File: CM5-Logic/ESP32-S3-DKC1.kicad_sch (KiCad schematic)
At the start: 9 parts, among them J5 SSW-120-01-G-S-LL, J8 SSW-120-01-G-S-LL

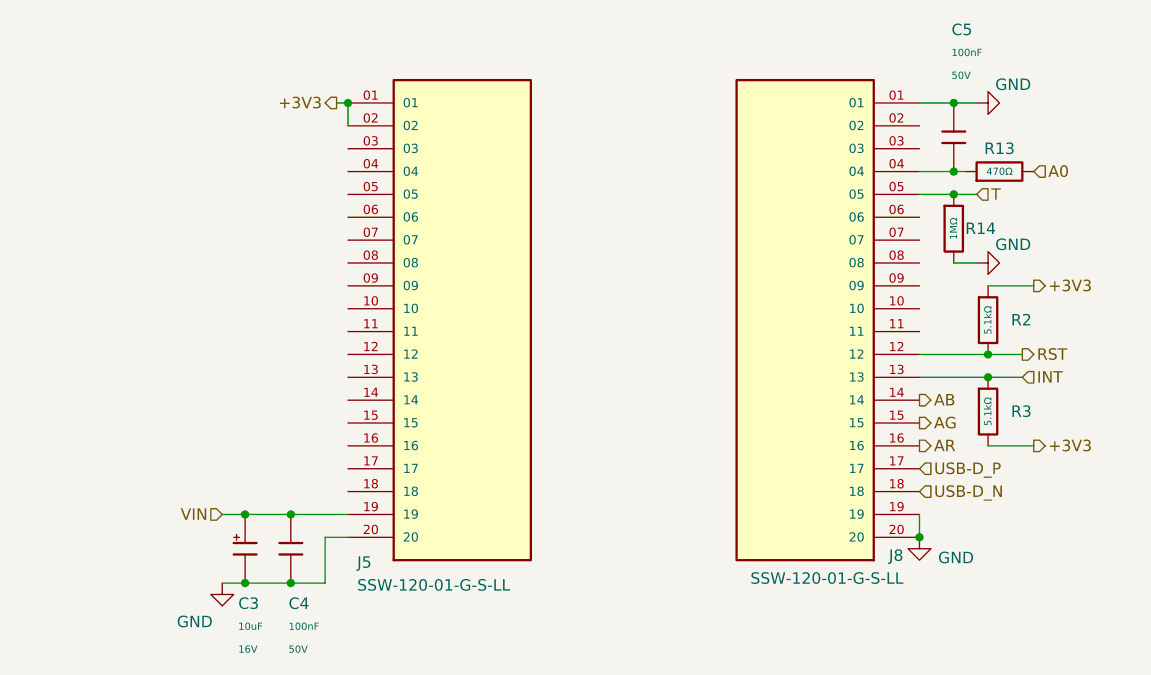
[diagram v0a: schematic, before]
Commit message: adds power connector and works on the ESP32 outputs
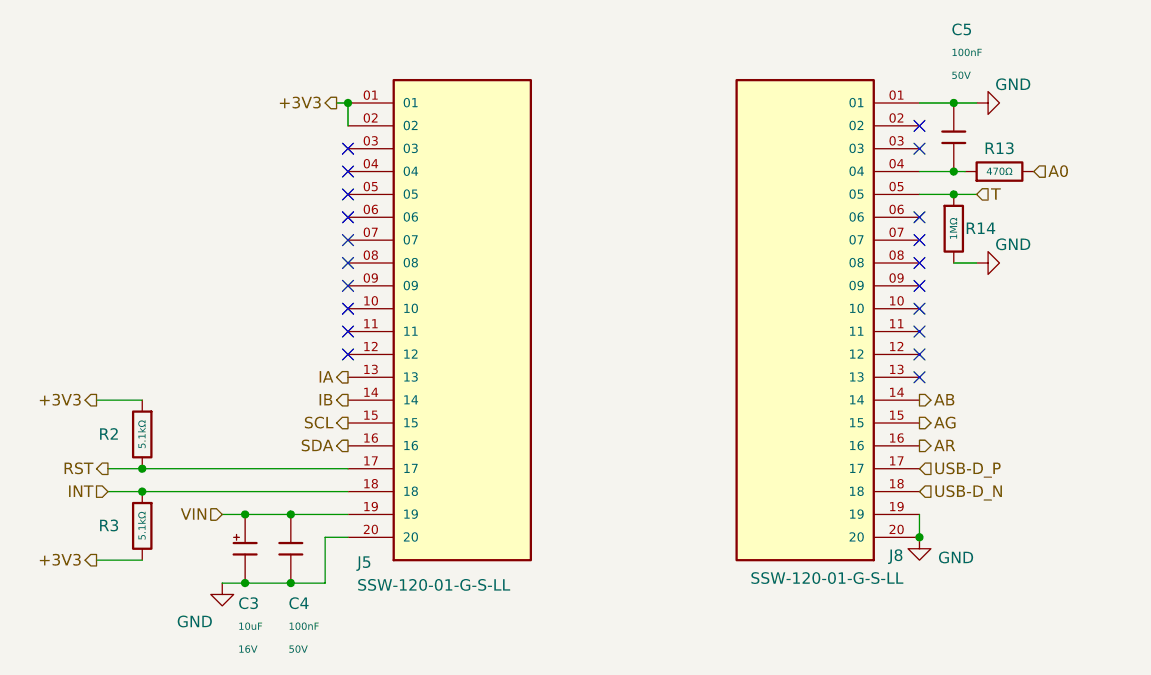
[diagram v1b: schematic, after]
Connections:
- net INT: now also J5.18; no longer J8.13
- net RST: now also J5.17; no longer J8.12
- net IA: now reaches J5.13
- net IB: now reaches J5.14
- net SCL: now reaches J5.15
- net SDA: now reaches J5.16
- no-connect marks 0 -> 20
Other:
- moved on the sheet: R2, R3

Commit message: adds a base motor driver with UART integration for the ESP32-S3-DC1 base hub
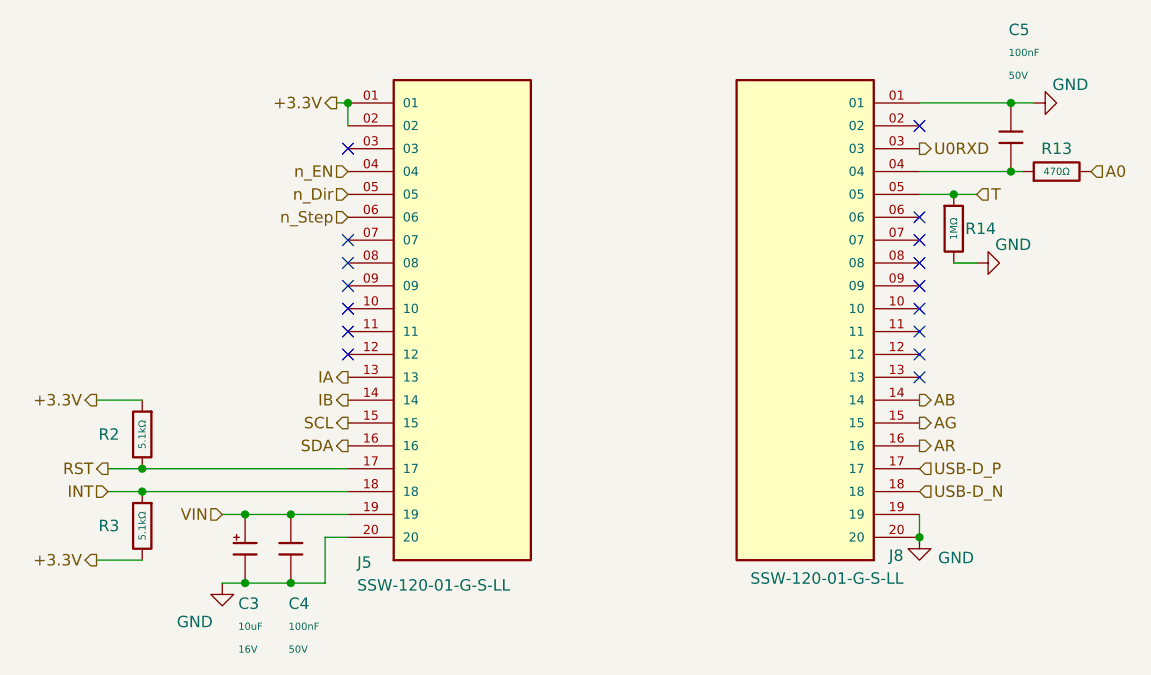
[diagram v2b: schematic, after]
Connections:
- net n_EN: now reaches J5.04
- net n_Dir: now reaches J5.05
- net n_Step: now reaches J5.06
- net U0RXD: now reaches J8.03
- net +3V3 renamed +3.3V
- no-connect marks 20 -> 16
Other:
- moved on the sheet: C5, R13

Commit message: changes USB port, adds TMC2209 SilentStepStick footprint, redoes PCB Layout
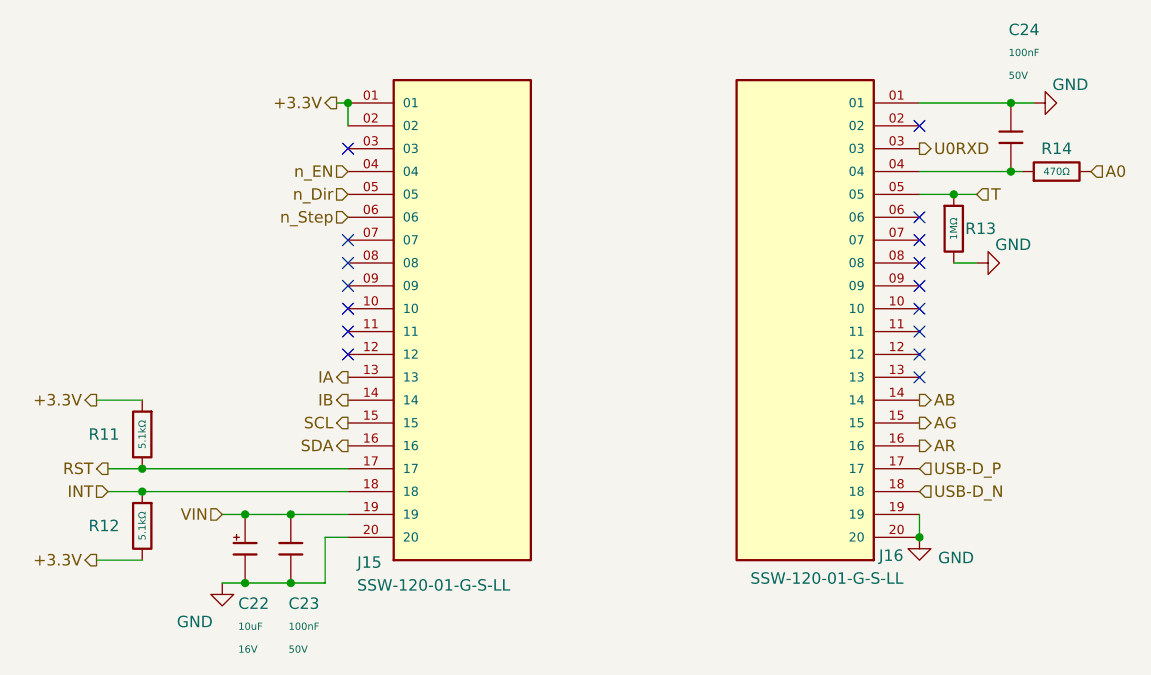
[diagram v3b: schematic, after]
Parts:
- renumbered C3 to C22, C4 to C23, C5 to C24, J5 to J15, J8 to J16, R2 to R11, R3 to R12, R14 to R13, R13 to R14
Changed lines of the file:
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@@
 		(on_board yes)
 		(dnp no)
-		(property "Reference" "R14"
+		(property "Reference" "R13"
 			(at 173.99 78.74 0)
 			(effects
@@
 			(project ""
 				(path "/e63e39d7-6ac0-4ffd-8aa3-1841a4541b55/15cde86c-493f-4d28-8a18-7dec09ac8995"
-					(reference "R14")
+					(reference "R13")
 					(unit 1)
 				)
@@
 		(on_board yes)
 		(dnp no)
-		(property "Reference" "#PWR012"
+		(property "Reference" "#PWR061"
 			(at 91.44 124.46 0)
 			(effects
@@
 			(project "CM5IO"
 				(path "/e63e39d7-6ac0-4ffd-8aa3-1841a4541b55/15cde86c-493f-4d28-8a18-7dec09ac8995"
-					(reference "#PWR012")
+					(reference "#PWR061")
 					(unit 1)
 				)
@@
 		(on_board yes)
 		(dnp no)
-		(property "Reference" "R13"
+		(property "Reference" "R14"
 			(at 184.15 69.85 90)
 			(effects
@@
 			(project ""
 				(path "/e63e39d7-6ac0-4ffd-8aa3-1841a4541b55/15cde86c-493f-4d28-8a18-7dec09ac8995"
-					(reference "R13")
+					(reference "R14")
 					(unit 1)
 				)
@@
 		(on_board yes)
 		(dnp no)
-		(property "Reference" "J5"
+		(property "Reference" "J15"
 			(at 106.426 115.824 0)
 			(effects
@@
 			(project ""
 				(path "/e63e39d7-6ac0-4ffd-8aa3-1841a4541b55/15cde86c-493f-4d28-8a18-7dec09ac8995"
-					(reference "J5")
+					(reference "J15")
 					(unit 1)
 				)
@@
 		(on_board yes)
 		(dnp no)
-		(property "Reference" "J8"
+		(property "Reference" "J16"
 			(at 167.132 115.062 0)
 			(effects
@@
 			(project "CM5IO"
 				(path "/e63e39d7-6ac0-4ffd-8aa3-1841a4541b55/15cde86c-493f-4d28-8a18-7dec09ac8995"
-					(reference "J8")
+					(reference "J16")
 					(unit 1)
 				)
@@
 		(on_board yes)
 		(dnp no)
-		(property "Reference" "#PWR011"
+		(property "Reference" "#PWR064"
 			(at 187.96 64.77 0)
 			(effects
@@
 			(project "CM5IO"
 				(path "/e63e39d7-6ac0-4ffd-8aa3-1841a4541b55/15cde86c-493f-4d28-8a18-7dec09ac8995"
-					(reference "#PWR011")
+					(reference "#PWR064")
 					(unit 1)
 				)
@@
 		(on_board yes)
 		(dnp no)
-		(property "Reference" "#PWR010"
+		(property "Reference" "#PWR062"
 			(at 168.91 119.38 0)
 			(effects
@@
 			(project ""
 				(path "/e63e39d7-6ac0-4ffd-8aa3-1841a4541b55/15cde86c-493f-4d28-8a18-7dec09ac8995"
-					(reference "#PWR010")
+					(reference "#PWR062")
 					(unit 1)
 				)
@@
 		(dnp no)
 		(fields_autoplaced yes)
-		(property "Reference" "R2"
+		(property "Reference" "R11"
 			(at 80.01 101.5999 0)
 			(effects
@@
 			(project "CM5IO"
 				(path "/e63e39d7-6ac0-4ffd-8aa3-1841a4541b55/15cde86c-493f-4d28-8a18-7dec09ac8995"
-					(reference "R2")
+					(reference "R11")
 					(unit 1)
 				)
@@
 		(on_board yes)
 		(dnp no)
-		(property "Reference" "C5"
+		(property "Reference" "C24"
 			(at 178.816 56.642 0)
 			(effects
@@
 			(project ""
 				(path "/e63e39d7-6ac0-4ffd-8aa3-1841a4541b55/15cde86c-493f-4d28-8a18-7dec09ac8995"
-					(reference "C5")
+					(reference "C24")
 					(unit 1)
 				)
@@
 		(on_board yes)
 		(dnp no)
-		(property "Reference" "C4"
+		(property "Reference" "C23"
 			(at 98.806 120.3959 0)
 			(effects
@@
 			(project ""
 				(path "/e63e39d7-6ac0-4ffd-8aa3-1841a4541b55/15cde86c-493f-4d28-8a18-7dec09ac8995"
-					(reference "C4")
+					(reference "C23")
 					(unit 1)
 				)
@@
 		(on_board yes)
 		(dnp no)
-		(property "Reference" "#PWR013"
+		(property "Reference" "#PWR063"
 			(at 181.61 82.55 0)
 			(effects
@@
 			(project "CM5IO"
 				(path "/e63e39d7-6ac0-4ffd-8aa3-1841a4541b55/15cde86c-493f-4d28-8a18-7dec09ac8995"
-					(reference "#PWR013")
+					(reference "#PWR063")
 					(unit 1)
 				)
@@
 		(dnp no)
 		(fields_autoplaced yes)
-		(property "Reference" "R3"
+		(property "Reference" "R12"
 			(at 80.01 111.7599 0)
 			(effects
@@
 			(project "CM5IO"
 				(path "/e63e39d7-6ac0-4ffd-8aa3-1841a4541b55/15cde86c-493f-4d28-8a18-7dec09ac8995"
-					(reference "R3")
+					(reference "R12")
 					(unit 1)
 				)
@@
 		(on_board yes)
 		(dnp no)
-		(property "Reference" "C3"
+		(property "Reference" "C22"
 			(at 93.218 120.3959 0)
 			(effects
@@
 			(project "CM5IO"
 				(path "/e63e39d7-6ac0-4ffd-8aa3-1841a4541b55/15cde86c-493f-4d28-8a18-7dec09ac8995"
-					(reference "C3")
+					(reference "C22")
 					(unit 1)
 				)
